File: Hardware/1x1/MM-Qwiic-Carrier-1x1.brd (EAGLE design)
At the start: 80 x 35.6 mm, 89 parts, among them J15 MICROMOD-2222-C, J2 QWIIC_RIGHT_ANGLE, J5 Vertical Qwiic Connector, U1 MCP73831, U5 AP7361C-33FGEUDFN-8

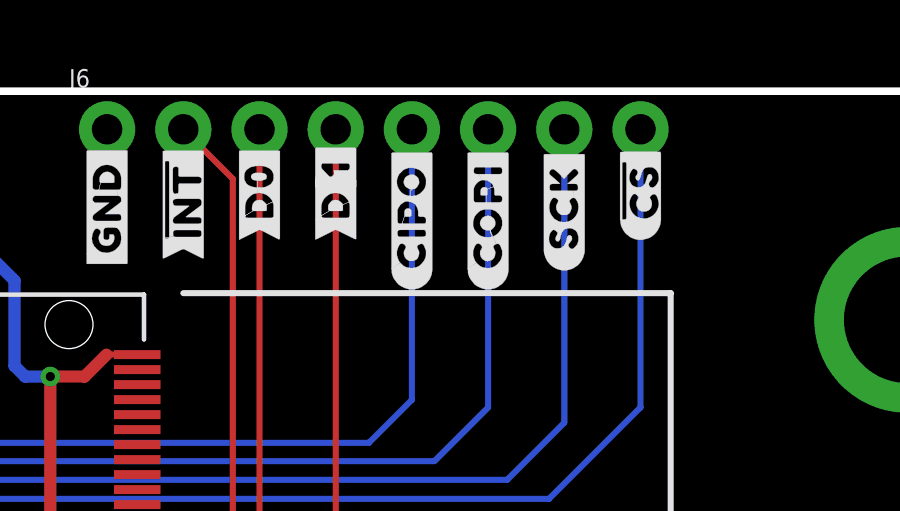
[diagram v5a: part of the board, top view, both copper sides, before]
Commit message: silk screen
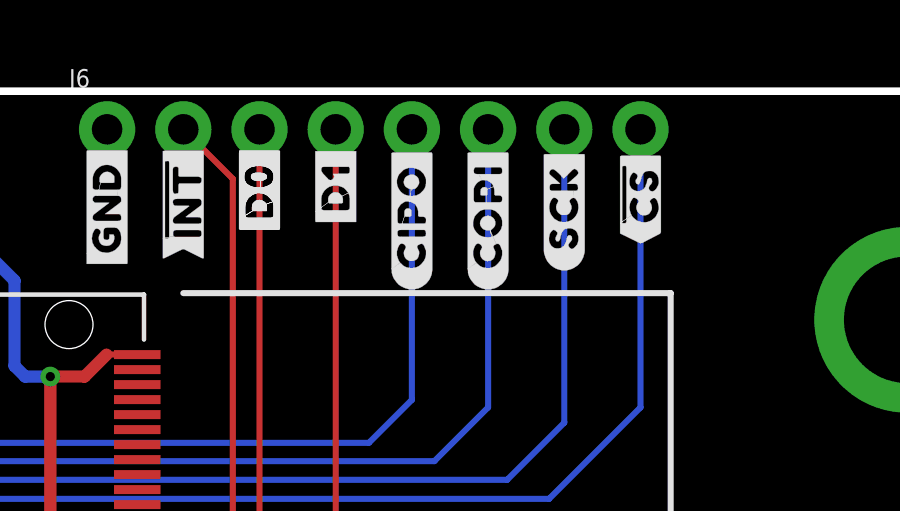
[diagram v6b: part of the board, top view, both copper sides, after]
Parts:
- removed U$30, U$31: (no value), output:#1#0
- U$20, U$21: device output:#D#0 -> output:#D1#0
- moved U$20 0.25 mm to (33.0, 30.9)
- moved U$21 0.25 mm to (33.0, 30.9)
- moved U$28 0.13 mm to (43.2, 30.5)
- moved U$29 0.13 mm to (43.2, 30.5)
- flipped U$18 to the top
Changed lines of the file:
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@@
 <?xml version="1.0" encoding="utf-8"?>
 <!DOCTYPE eagle SYSTEM "eagle.dtd">
-<eagle version="9.5.2">
+<eagle version="9.6.2">
 <drawing>
 <settings>
@@
 <element name="U$15" library="output" package="##INT##0" value="" x="27.94" y="29.972" smashed="yes" rot="R90"/>
 <element name="U$16" library="output" package="##INT##0" value="" x="27.94" y="29.972" smashed="yes" rot="MR90"/>
-<element name="U$17" library="output" package="#D0#0" value="" x="30.48" y="30.607" smashed="yes" rot="R90"/>
-<element name="U$18" library="output" package="#D0#0" value="" x="30.48" y="30.607" smashed="yes" rot="MR90"/>
 <element name="U$22" library="output" package="#CIPO#0" value="" x="35.56" y="28.956" smashed="yes" rot="R90"/>
 <element name="U$23" library="output" package="#CIPO#0" value="" x="35.56" y="28.956" smashed="yes" rot="MR90"/>
@@
 <element name="U$26" library="output" package="#SCK#0" value="" x="40.64" y="29.591" smashed="yes" rot="R90"/>
 <element name="U$27" library="output" package="#SCK#0" value="" x="40.64" y="29.591" smashed="yes" rot="MR90"/>
-<element name="U$28" library="output" package="##CS##0" value="" x="43.18" y="30.607" smashed="yes" rot="R90"/>
-<element name="U$29" library="output" package="##CS##0" value="" x="43.18" y="30.607" smashed="yes" rot="MR90"/>
-<element name="U$20" library="output" package="#D#0" value="" x="33.02" y="30.607" smashed="yes" rot="R90"/>
-<element name="U$21" library="output" package="#D#0" value="" x="33.02" y="30.607" smashed="yes" rot="MR90"/>
-<element name="U$30" library="output" package="#1#0" value="" x="33.02" y="32.004" smashed="yes" rot="R90"/>
-<element name="U$31" library="output" package="#1#0" value="" x="33.02" y="32.004" smashed="yes" rot="MR90"/>
 <element name="U$12" library="output" package="#VBAT#0" value="" x="7.366" y="19.685" smashed="yes" rot="MR0"/>
 <element name="U$33" library="output" package="#GND#0" value="" x="6.096" y="17.145" smashed="yes" rot="MR0"/>
@@
 <element name="U$36" library="buzzard_labels (1)" package="#0" value="" x="1.143" y="17.399" smashed="yes"/>
 <element name="U$37" library="buzzard_labels (1)" package="#0" value="" x="7.366" y="23.495" smashed="yes"/>
+<element name="U$17" library="output" package="#D0#0" value="" x="30.48" y="30.607" smashed="yes" rot="R90"/>
+<element name="U$18" library="output" package="#D0#0" value="" x="30.48" y="30.607" smashed="yes" rot="R90"/>
+<element name="U$20" library="output" package="#D1#0" value="" x="33.02" y="30.861" smashed="yes" rot="R90"/>
+<element name="U$21" library="output" package="#D1#0" value="" x="33.02" y="30.861" smashed="yes" rot="MR90"/>
+<element name="U$28" library="output" package="##CS##0" value="" x="43.18" y="30.48" smashed="yes" rot="R90"/>
+<element name="U$29" library="output" package="##CS##0" value="" x="43.18" y="30.48" smashed="yes" rot="MR90"/>
 </elements>
 <signals>
